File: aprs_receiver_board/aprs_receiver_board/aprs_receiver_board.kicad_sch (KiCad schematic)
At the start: 0 parts

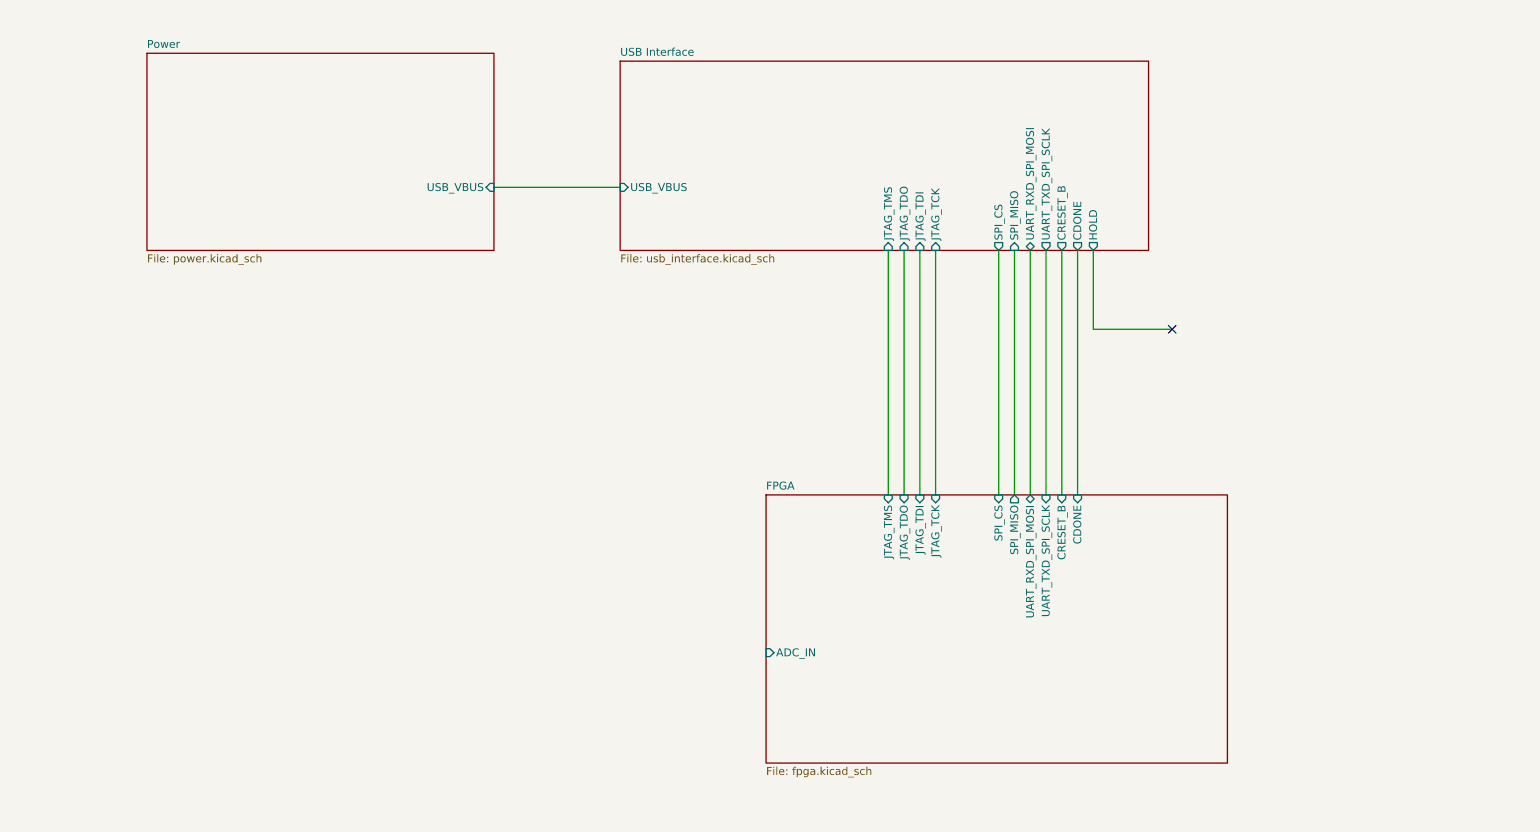
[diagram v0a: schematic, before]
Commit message: Add decoupling capacitor and IO connectors
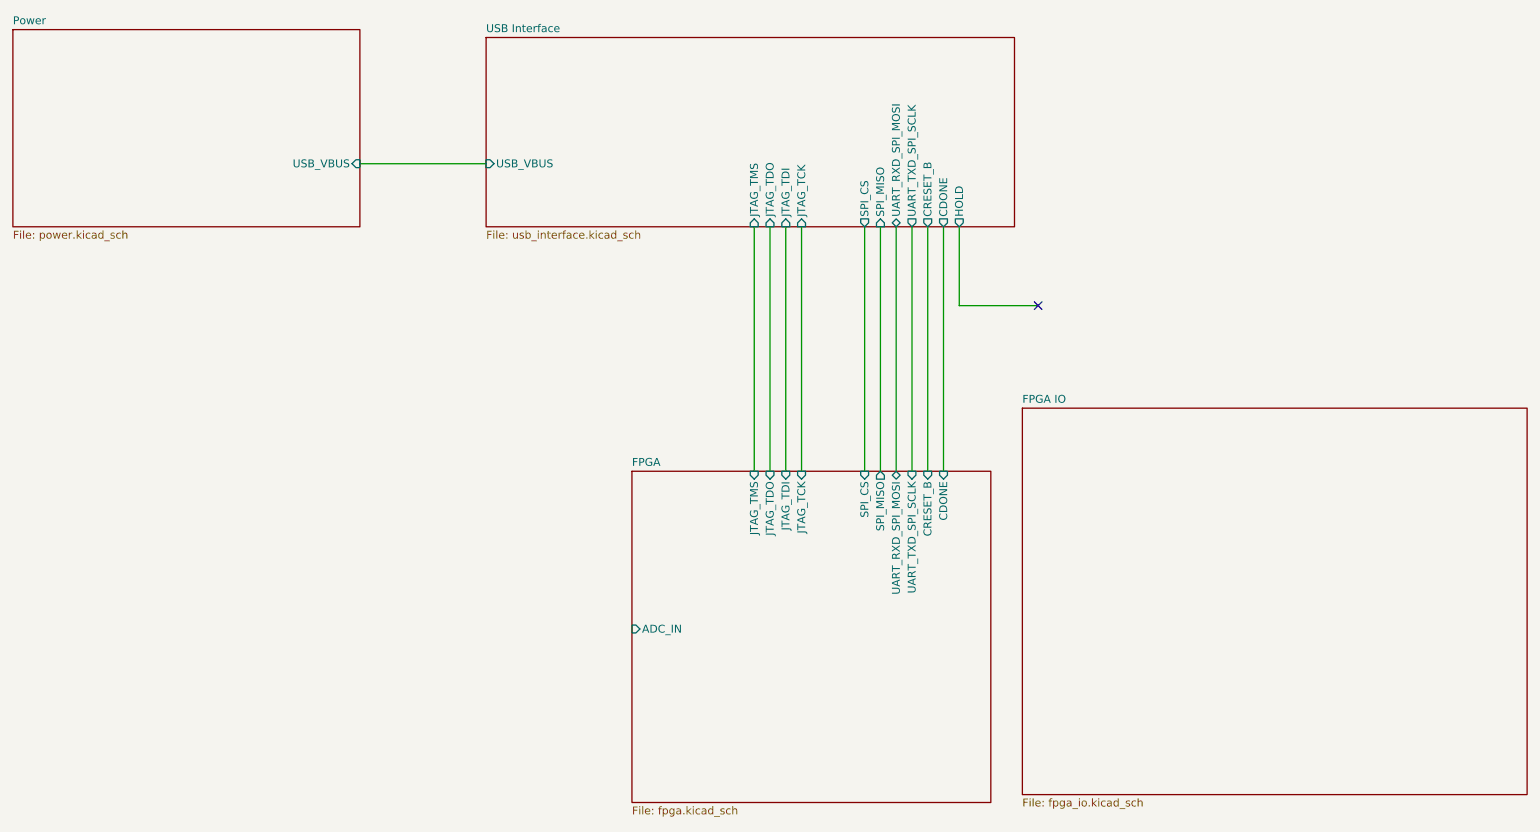
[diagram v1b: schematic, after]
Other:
- added sheet FPGA IO (fpga_io.kicad_sch)
